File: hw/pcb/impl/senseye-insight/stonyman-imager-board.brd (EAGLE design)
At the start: 16.4 x 14.9 mm, 8 parts

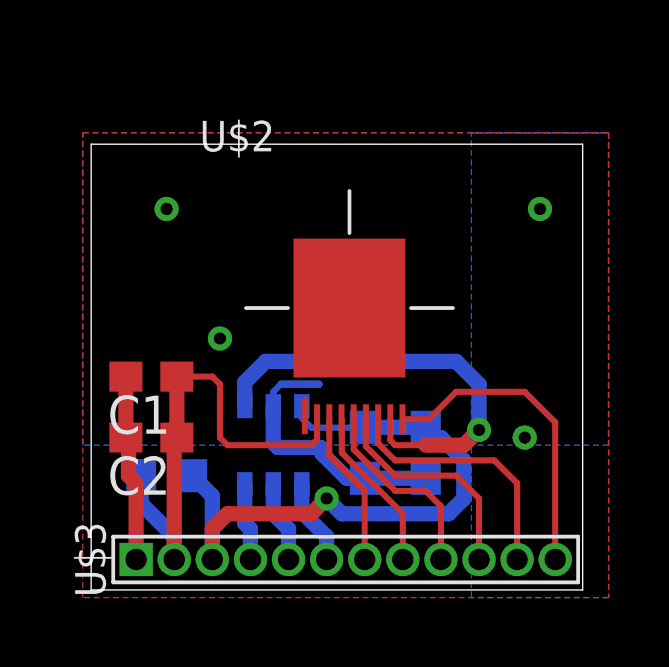
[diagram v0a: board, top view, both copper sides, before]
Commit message: created tiny imager adc board
started over with a new board for the stonyman imager and ADC (same
schematic).  It is completely routed and passes the DRC with the
Sunstone 2 layer DRU file.  It still needs drill holes for the lens
mount, and silkscreen.
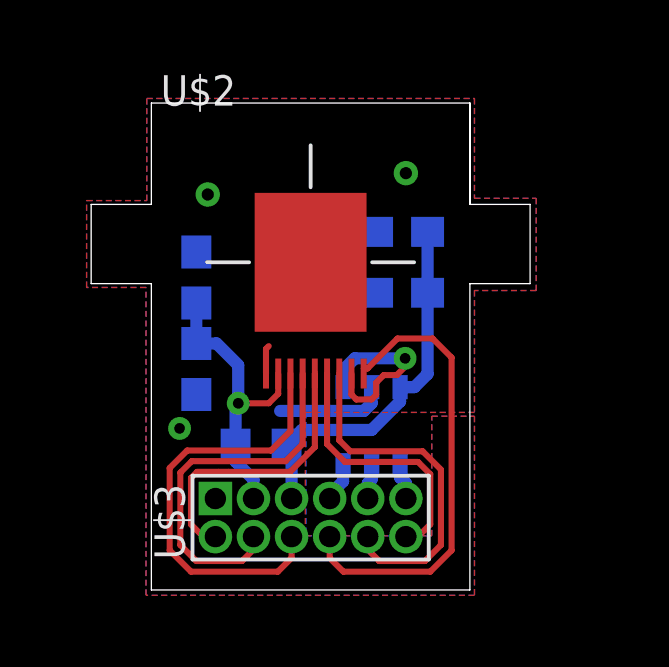
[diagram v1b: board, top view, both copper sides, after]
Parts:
- U$3: value HEADER_12PIN1X12 -> HEADER_12PIN2X6; device senseye:HEADER1X12/0.05IN -> senseye:HEADER2X6/0.05IN
- moved C3 7.41 mm to (10.4, 11.9), turned to 180 degrees
- moved C4 5.48 mm to (10.4, 9.91), turned to 180 degrees
- moved C1 3.63 mm to (3.51, 10.4), flipped to the bottom, turned to 90 degrees
- moved U$1 3.34 mm to (9.35, 5.46)
- moved R1 3.31 mm to (5.66, 4.83)
- moved C2 2.73 mm to (3.51, 7.37), flipped to the bottom, turned to 270 degrees
- moved U$3 2.28 mm to (7.32, 2.41)
- moved U$2 2.00 mm to (7.32, 10.9)
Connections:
- net ADC-MISO: now also U$3.9; no longer U$3.5
- net ADC-SCLK: now also U$3.11; no longer U$3.6
- net ADC-SS: now also U$3.7; no longer U$3.4
- net INCP: now also U$3.4; no longer U$3.8
- net INCV: now also U$3.12; no longer U$3.10
- net INPHI: now also U$3.10; no longer U$3.11
- net OENABLE: now also U$3.8; no longer U$3.12
- net RESP: now also U$3.6; no longer U$3.7
- net RESV: now also U$3.2; no longer U$3.9
- net V_ADC: now also U$3.5; no longer U$3.3
- net V_STONY: now also U$3.3; no longer U$3.2
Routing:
- net GND: track 15.9 -> 4.64 mm, vias 4 -> 3
- net RESP: track 5.16 -> 14.5 mm
- net V_ADC: track 21.0 -> 12.5 mm, vias 1 -> 0
- net ANALOG: track 14.7 -> 6.33 mm
- net INCP: track 5.50 -> 12.5 mm
- net V_STONY: track 16.8 -> 9.91 mm, vias 0 -> 1
- net OENABLE: track 10.5 -> 15.3 mm
- net INPHI: track 8.53 -> 11.8 mm
- net RESV: track 6.47 -> 9.54 mm
- net ADC-SCLK: track 2.85 -> 1.19 mm
- net ADC-MISO: track 2.72 -> 1.17 mm
- net INCV: track 7.43 -> 8.86 mm
- net ADC-SS: track 2.59 -> 1.30 mm
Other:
- board size 16.4 x 14.9 mm -> 14.6 x 16.2 mm

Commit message: moved two caps to make bottom ground plane connect
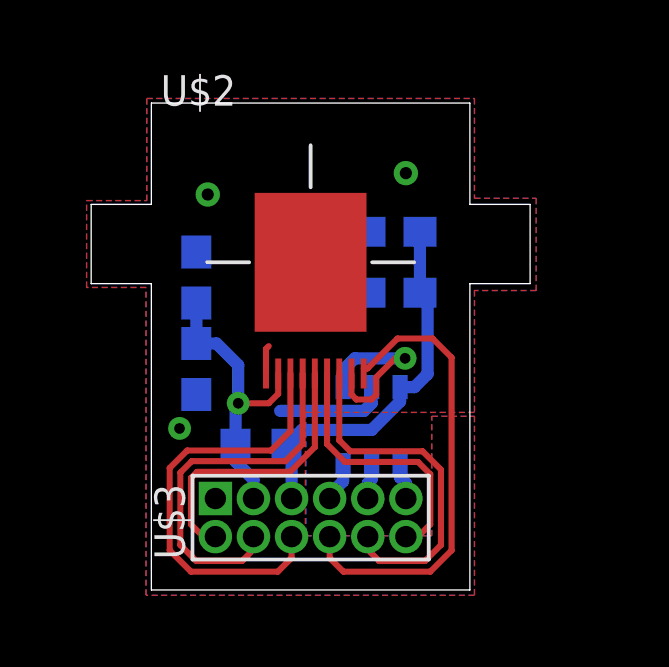
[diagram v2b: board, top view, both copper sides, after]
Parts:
- moved C3 0.25 mm to (10.1, 11.9)
- moved C4 0.25 mm to (10.1, 9.91)
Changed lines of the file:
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@@
 <setting verticaltext="up"/>
 </settings>
-<grid distance="0.1" unitdist="inch" unit="inch" style="lines" multiple="1" display="yes" altdistance="0.001" altunitdist="inch" altunit="inch"/>
+<grid distance="0.1" unitdist="inch" unit="inch" style="lines" multiple="1" display="yes" altdistance="0.005" altunitdist="inch" altunit="inch"/>
 <layers>
 <layer number="1" name="Top" color="4" fill="1" visible="yes" active="yes"/>
@@
 <wire x1="14.6304" y1="10.2108" x2="14.6304" y2="12.8524" width="0" layer="20"/>
 <wire x1="14.6304" y1="12.8524" x2="12.6238" y2="12.8524" width="0" layer="20"/>
-<wire x1="12.6238" y1="12.8524" x2="12.6238" y2="16.2306" width="0" layer="20"/>
 <wire x1="12.6238" y1="16.2306" x2="2.0066" y2="16.2306" width="0" layer="20"/>
 <wire x1="2.0066" y1="16.2306" x2="2.0066" y2="12.8524" width="0" layer="20"/>
@@
 <element name="C1" library="rcl" package="C0603" value="1nF" x="3.5052" y="10.414" rot="MR90"/>
 <element name="C2" library="rcl" package="C0603" value="0.1uF" x="3.5052" y="7.366" rot="MR270"/>
-<element name="C3" library="rcl" package="C0603" value="0.1uF" x="10.3632" y="11.938" rot="MR180"/>
-<element name="C4" library="rcl" package="C0603" value="1uF" x="10.3632" y="9.906" rot="MR180"/>
+<element name="C3" library="rcl" package="C0603" value="0.1uF" x="10.1092" y="11.938" rot="MR180"/>
+<element name="C4" library="rcl" package="C0603" value="1uF" x="10.1092" y="9.906" rot="MR180"/>
 <element name="R1" library="rcl" package="R0603" value="0 or UNPOP" x="5.6642" y="4.826" rot="MR0"/>
 <element name="U$2" library="senseye" package="STONYMAN_DEFAULT_LENS" value="STONYMANDEFAULT_LENS_MOUNT" x="7.3152" y="10.922"/>
@@
 <wire x1="10.2972" y1="6.761" x2="10.7742" y2="6.761" width="0.4064" layer="16"/>
 <wire x1="10.7742" y1="6.761" x2="11.2132" y2="7.2" width="0.4064" layer="16"/>
-<wire x1="11.2132" y1="7.2" x2="11.2132" y2="11.938" width="0.4064" layer="16"/>
-<wire x1="11.2132" y1="11.938" x2="11.2132" y2="9.906" width="0" layer="19" extent="16-16"/>
+<wire x1="11.2132" y1="7.2" x2="11.2132" y2="9.652" width="0.4064" layer="16"/>
+<wire x1="11.2132" y1="9.652" x2="10.9592" y2="9.906" width="0.4064" layer="16"/>
+<wire x1="10.9592" y1="11.938" x2="10.9592" y2="9.906" width="0.4064" layer="16"/>
 </signal>
 <signal name="ANALOG">
@@
 <wire x1="8.8392" y1="6.35" x2="9.3472" y2="6.35" width="0.2032" layer="1"/>
 <wire x1="9.3472" y1="6.35" x2="9.4996" y2="6.5024" width="0.2032" layer="1"/>
-<wire x1="9.4996" y1="6.5024" x2="9.4996" y2="6.9088" width="0.2032" layer="1"/>
-<wire x1="9.4996" y1="6.9088" x2="9.7536" y2="7.1628" width="0.2032" layer="1"/>
-<wire x1="9.7536" y1="7.1628" x2="10.1854" y2="7.1628" width="0.2032" layer="1"/>
-<wire x1="10.1854" y1="7.1628" x2="10.4648" y2="7.4422" width="0.2032" layer="1"/>
-<wire x1="10.4648" y1="7.4422" x2="10.4648" y2="7.7216" width="0.2032" layer="1"/>
+<wire x1="9.4996" y1="6.5024" x2="9.4996" y2="7.0866" width="0.2032" layer="1"/>
 <wire x1="8.3972" y1="6.761" x2="8.3972" y2="7.3304" width="0.4064" layer="16"/>
 <wire x1="8.7884" y1="7.7216" x2="10.4648" y2="7.7216" width="0.4064" layer="16"/>
 <wire x1="8.3972" y1="7.3304" x2="8.7884" y2="7.7216" width="0.4064" layer="16"/>
+<wire x1="9.4996" y1="7.0866" x2="10.1346" y2="7.7216" width="0.2032" layer="1"/>
+<wire x1="10.1346" y1="7.7216" x2="10.4648" y2="7.7216" width="0.2032" layer="1"/>
 </signal>
 <signal name="ADC-MISO">

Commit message: rounded board inner corners with miter tool
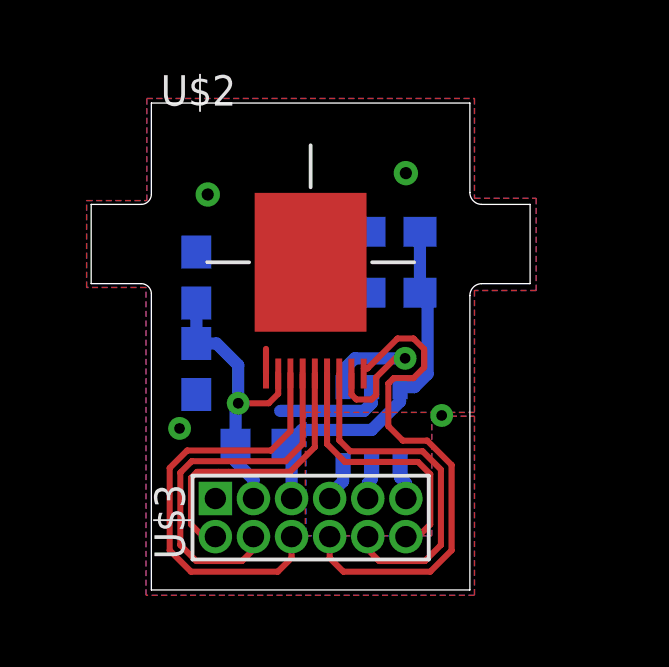
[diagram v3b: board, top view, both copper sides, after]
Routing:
- net OENABLE: track 15.3 -> 16.8 mm
- net GND: track 4.64 -> 4.51 mm, vias 3 -> 4
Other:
- outline, holes or cut-outs redrawn
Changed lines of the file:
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@@
 <setting verticaltext="up"/>
 </settings>
-<grid distance="0.1" unitdist="inch" unit="inch" style="lines" multiple="1" display="yes" altdistance="0.005" altunitdist="inch" altunit="inch"/>
+<grid distance="0.1" unitdist="inch" unit="inch" style="lines" multiple="1" display="yes" altdistance="0.001" altunitdist="inch" altunit="inch"/>
 <layers>
 <layer number="1" name="Top" color="4" fill="1" visible="yes" active="yes"/>
@@
 <plain>
 <wire x1="2.0066" y1="0" x2="12.6238" y2="0" width="0" layer="20"/>
-<wire x1="12.6238" y1="10.2108" x2="14.6304" y2="10.2108" width="0" layer="20"/>
+<wire x1="12.6238" y1="0" x2="12.6238" y2="9.814040625" width="0" layer="20"/>
+<wire x1="12.6238" y1="9.814040625" x2="13.020559375" y2="10.2108" width="0" layer="20" curve="-90"/>
+<wire x1="13.020559375" y1="10.2108" x2="14.6304" y2="10.2108" width="0" layer="20"/>
 <wire x1="14.6304" y1="10.2108" x2="14.6304" y2="12.8524" width="0" layer="20"/>
-<wire x1="14.6304" y1="12.8524" x2="12.6238" y2="12.8524" width="0" layer="20"/>
+<wire x1="14.6304" y1="12.8524" x2="13.01893125" y2="12.8524" width="0" layer="20"/>
+<wire x1="13.01893125" y1="12.8524" x2="12.6238" y2="13.24753125" width="0" layer="20" curve="-90"/>
+<wire x1="12.6238" y1="13.24753125" x2="12.6238" y2="16.2306" width="0" layer="20"/>
 <wire x1="12.6238" y1="16.2306" x2="2.0066" y2="16.2306" width="0" layer="20"/>
-<wire x1="2.0066" y1="16.2306" x2="2.0066" y2="12.8524" width="0" layer="20"/>
-<wire x1="2.0066" y1="12.8524" x2="0" y2="12.8524" width="0" layer="20"/>
+<wire x1="2.0066" y1="16.2306" x2="2.0066" y2="13.194121875" width="0" layer="20"/>
+<wire x1="2.0066" y1="13.194121875" x2="1.664878125" y2="12.8524" width="0" layer="20" curve="-90"/>
+<wire x1="1.664878125" y1="12.8524" x2="0" y2="12.8524" width="0" layer="20"/>
 <wire x1="0" y1="12.8524" x2="0" y2="10.2108" width="0" layer="20"/>
-<wire x1="0" y1="10.2108" x2="2.0066" y2="10.2108" width="0" layer="20"/>
-<wire x1="2.0066" y1="10.2108" x2="2.0066" y2="0" width="0" layer="20"/>
-<wire x1="12.6238" y1="0" x2="12.6238" y2="10.2108" width="0" layer="20"/>
-<wire x1="12.6238" y1="12.8524" x2="12.6238" y2="16.2306" width="0" layer="20"/>
+<wire x1="0" y1="10.2108" x2="1.664878125" y2="10.2108" width="0" layer="20"/>
+<wire x1="1.664878125" y1="10.2108" x2="2.0066" y2="9.869078125" width="0" layer="20" curve="-90"/>
+<wire x1="2.0066" y1="9.869078125" x2="2.0066" y2="0" width="0" layer="20"/>
 </plain>
 <attributes>
@@
 <via x="10.4902" y="13.8938" extent="1-16" drill="0.4064"/>
 <wire x1="5.8278" y1="7.2146" x2="5.8278" y2="8.0376" width="0.2032" layer="1"/>
-<wire x1="5.8278" y1="8.0376" x2="5.9182" y2="8.128" width="0.2032" layer="1"/>
 <via x="3.8862" y="13.1826" extent="1-16" drill="0.4064"/>
 <polygon width="0.2032" layer="1" isolate="0.3048">
@@
 <vertex x="1.8542" y="12.9794"/>
 </polygon>
+<via x="11.684" y="5.8166" extent="1-16" drill="0.3556" diameter="0.254"/>
 </signal>
 <signal name="V_STONY">
@@
 <contactref element="U$2" pad="P$9"/>
 <contactref element="U$3" pad="8"/>
-<wire x1="11.3792" y1="8.382" x2="12.0142" y2="7.747" width="0.2032" layer="1"/>
-<wire x1="12.0142" y1="7.747" x2="12.0142" y2="1.3208" width="0.2032" layer="1"/>
+<wire x1="12.0142" y1="4.1656" x2="12.0142" y2="1.3208" width="0.2032" layer="1"/>
 <wire x1="12.0142" y1="1.3208" x2="11.303" y2="0.6096" width="0.2032" layer="1"/>
 <wire x1="11.303" y1="0.6096" x2="8.4074" y2="0.6096" width="0.2032" layer="1"/>
@@
 <wire x1="9.0838" y1="7.382" x2="9.2108" y2="7.382" width="0.2032" layer="1"/>
 <wire x1="9.2108" y1="7.382" x2="10.2108" y2="8.382" width="0.2032" layer="1"/>
-<wire x1="10.2108" y1="8.382" x2="11.3792" y2="8.382" width="0.2032" layer="1"/>
+<wire x1="10.2108" y1="8.382" x2="10.7442" y2="8.382" width="0.2032" layer="1"/>
+<wire x1="10.7442" y1="8.382" x2="11.0998" y2="8.0264" width="0.2032" layer="1"/>
+<wire x1="11.0998" y1="8.0264" x2="11.0998" y2="7.4168" width="0.2032" layer="1"/>
+<wire x1="11.0998" y1="7.4168" x2="10.7442" y2="7.0612" width="0.2032" layer="1"/>
+<wire x1="10.7442" y1="7.0612" x2="10.0838" y2="7.0612" width="0.2032" layer="1"/>
+<wire x1="10.0838" y1="7.0612" x2="9.906" y2="6.8834" width="0.2032" layer="1"/>
+<wire x1="9.906" y1="6.8834" x2="9.906" y2="5.461" width="0.2032" layer="1"/>
+<wire x1="9.906" y1="5.461" x2="10.3886" y2="4.9784" width="0.2032" layer="1"/>
+<wire x1="10.3886" y1="4.9784" x2="11.2014" y2="4.9784" width="0.2032" layer="1"/>
+<wire x1="11.2014" y1="4.9784" x2="12.0142" y2="4.1656" width="0.2032" layer="1"/>
 <wire x1="9.0838" y1="7.382" x2="9.0838" y2="7.2146" width="0" layer="19" extent="1-1"/>
 </signal>

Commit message: added labels to header and caps and resistor
updated the SensEye Eagle library to have prefixes for parts.  there
might be other changes to the LBR file which I forgot to commit
previously
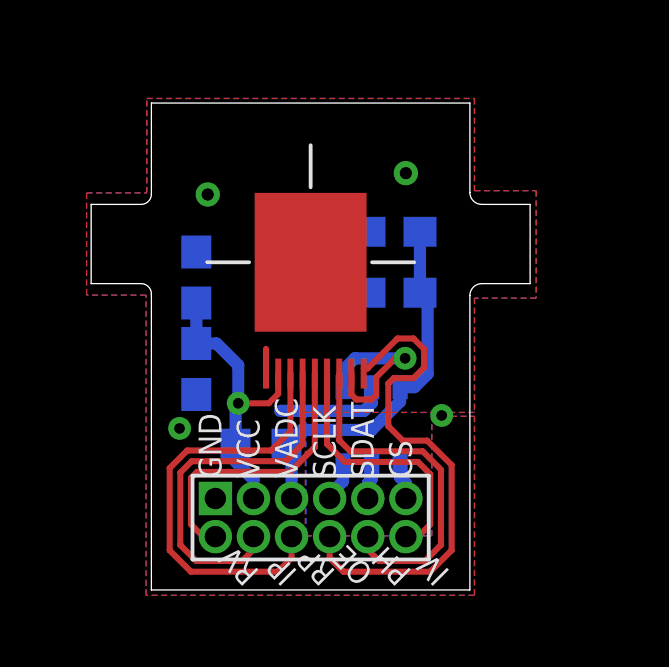
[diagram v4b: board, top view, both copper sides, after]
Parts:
- renumbered U$1 to U2, U$2 to U1, U$3 to J1
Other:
- board text added: "CS"
- board text added: "GND"
- board text added: "IP"
- board text added: "IV"
- board text added: "OE"
- board text added: "PH"
- board text added: "RP"
- board text added: "RV"
- board text added: "SCLK"
- board text added: "SDAT"
- board text added: "VADC"
- board text added: "VCC"
